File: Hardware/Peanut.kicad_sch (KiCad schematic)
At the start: 1 part

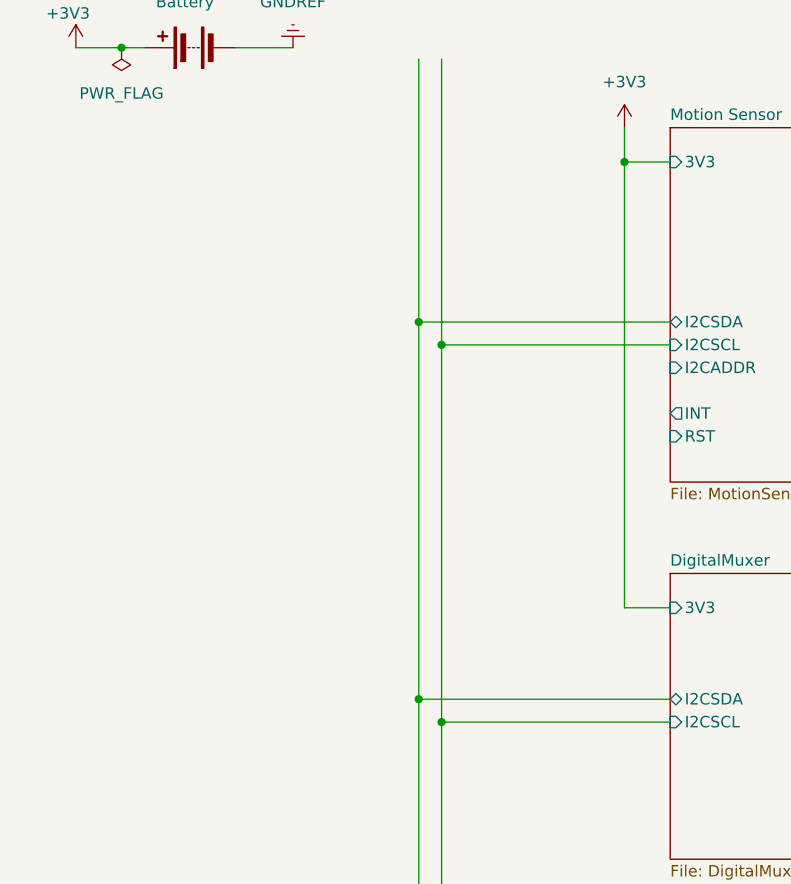
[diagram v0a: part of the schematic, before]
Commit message: Add Temperature and Humidity Sensor
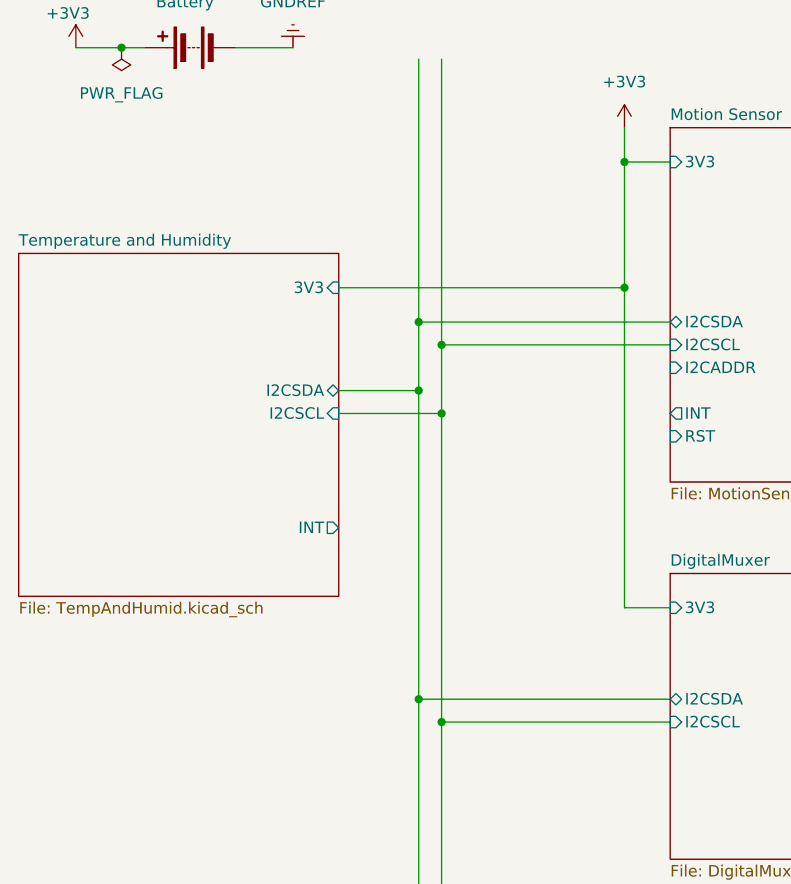
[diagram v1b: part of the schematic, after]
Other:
- added sheet Temperature and Humidity (TempAndHumid.kicad_sch)
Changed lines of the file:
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@@
+	)
+	(junction
+		(at 109.22 85.09)
+		(diameter 0)
+		(color 0 0 0 0)
+	)
+	(junction
+		(at 106.68 82.55)
+		(diameter 0)
+		(color 0 0 0 0)
+	)
+	(junction
+		(at 129.54 71.12)
+		(diameter 0)
+		(color 0 0 0 0)
 	)
 	(junction
@@
 	(wire
 		(pts
-			(xy 129.54 106.68) (xy 129.54 57.15)
+			(xy 97.79 71.12) (xy 129.54 71.12)
+		)
+		(stroke
+			(width 0)
+			(type default)
+		)
+	)
+	(wire
+		(pts
+			(xy 129.54 57.15) (xy 129.54 71.12)
 		)
 		(stroke
@@
 	(wire
 		(pts
+			(xy 97.79 82.55) (xy 106.68 82.55)
+		)
+		(stroke
+			(width 0)
+			(type default)
+		)
+	)
+	(wire
+		(pts
 			(xy 106.68 45.72) (xy 106.68 74.93)
 		)
@@
 	(wire
 		(pts
-			(xy 106.68 74.93) (xy 106.68 116.84)
+			(xy 106.68 74.93) (xy 106.68 82.55)
 		)
 		(stroke
@@
 	(wire
 		(pts
+			(xy 106.68 82.55) (xy 106.68 116.84)
+		)
+		(stroke
+			(width 0)
+			(type default)
+		)
+	)
+	(wire
+		(pts
+			(xy 129.54 71.12) (xy 129.54 106.68)
+		)
+		(stroke
+			(width 0)
+			(type default)
+		)
+	)
+	(wire
+		(pts
+			(xy 109.22 85.09) (xy 109.22 77.47)
+		)
+		(stroke
+			(width 0)
+			(type default)
+		)
+	)
+	(wire
+		(pts
 			(xy 134.62 106.68) (xy 129.54 106.68)
 		)
@@
 	(wire
 		(pts
+			(xy 97.79 85.09) (xy 109.22 85.09)
+		)
+		(stroke
+			(width 0)
+			(type default)
+		)
+	)
+	(wire
+		(pts
 			(xy 134.62 119.38) (xy 109.22 119.38)
 		)
@@
 	(wire
 		(pts
-			(xy 109.22 119.38) (xy 109.22 77.47)
+			(xy 109.22 85.09) (xy 109.22 119.38)
 		)
 		(stroke
@@
 				)
 			)
+		)
+	)
+	(sheet
+		(at 62.23 67.31)
+		(size 35.56 38.1)
+		(fields_autoplaced yes)
+		(stroke
+			(width 0.1524)
+			(type solid)
+		)
+		(fill
+			(color 255 229 191 1.0000)
+		)
+		(property "Sheetname" "Temperature and Humidity"
+			(at 62.23 66.5984 0)
+			(effects
+				(font
+					(size 1.27 1.27)
+				)
+				(justify left bottom)
+			)
+		)
+		(property "Sheetfile" "TempAndHumid.kicad_sch"
+			(at 62.23 105.9946 0)
+			(effects
+				(font
+					(size 1.27 1.27)
+				)
+				(justify left top)
+			)
+		)
+		(pin "3V3" input
+			(at 97.79 71.12 0)
+			(effects
+				(font
+					(size 1.27 1.27)
+				)
+				(justify right)
+			)
+		)
+		(pin "INT" output
+			(at 97.79 97.79 0)
+			(effects
+				(font
+					(size 1.27 1.27)
+				)
+				(justify right)
+			)
+		)
+		(pin "I2CSCL" input
+			(at 97.79 85.09 0)
+			(effects
+				(font
+					(size 1.27 1.27)
+				)
+				(justify right)
+			)
+		)
+		(pin "I2CSDA" bidirectional
+			(at 97.79 82.55 0)
+			(effects
+				(font
+					(size 1.27 1.27)
+				)
+				(justify right)
+			)
+		)
+		(instances
+			(project "Peanut"
+				(path "/298ef215-2a76-4225-b9ba-26c57869f278"
+					(page "4")
+				)
+			)

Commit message: Ambient Light Sensor
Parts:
- added J1: Conn_02x04_Odd_Even, symbol Connector_Generic:Conn_02x04_Odd_Even
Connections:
- net +3V3: now also J1.8 (Pin_8)
- net DigitalMuxer/I2CSCL: now also J1.4 (Pin_4)
- net DigitalMuxer/I2CSDA: now also J1.3 (Pin_3)
- new net GND: J1.1 (Pin_1)
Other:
- added sheet Light Sensor (LightSensor.kicad_sch)
- note added: "BOOT"
- note added: "RST"
- note added: "This is wrong"
- note added: "UART RX"
- note added: "UART TX"

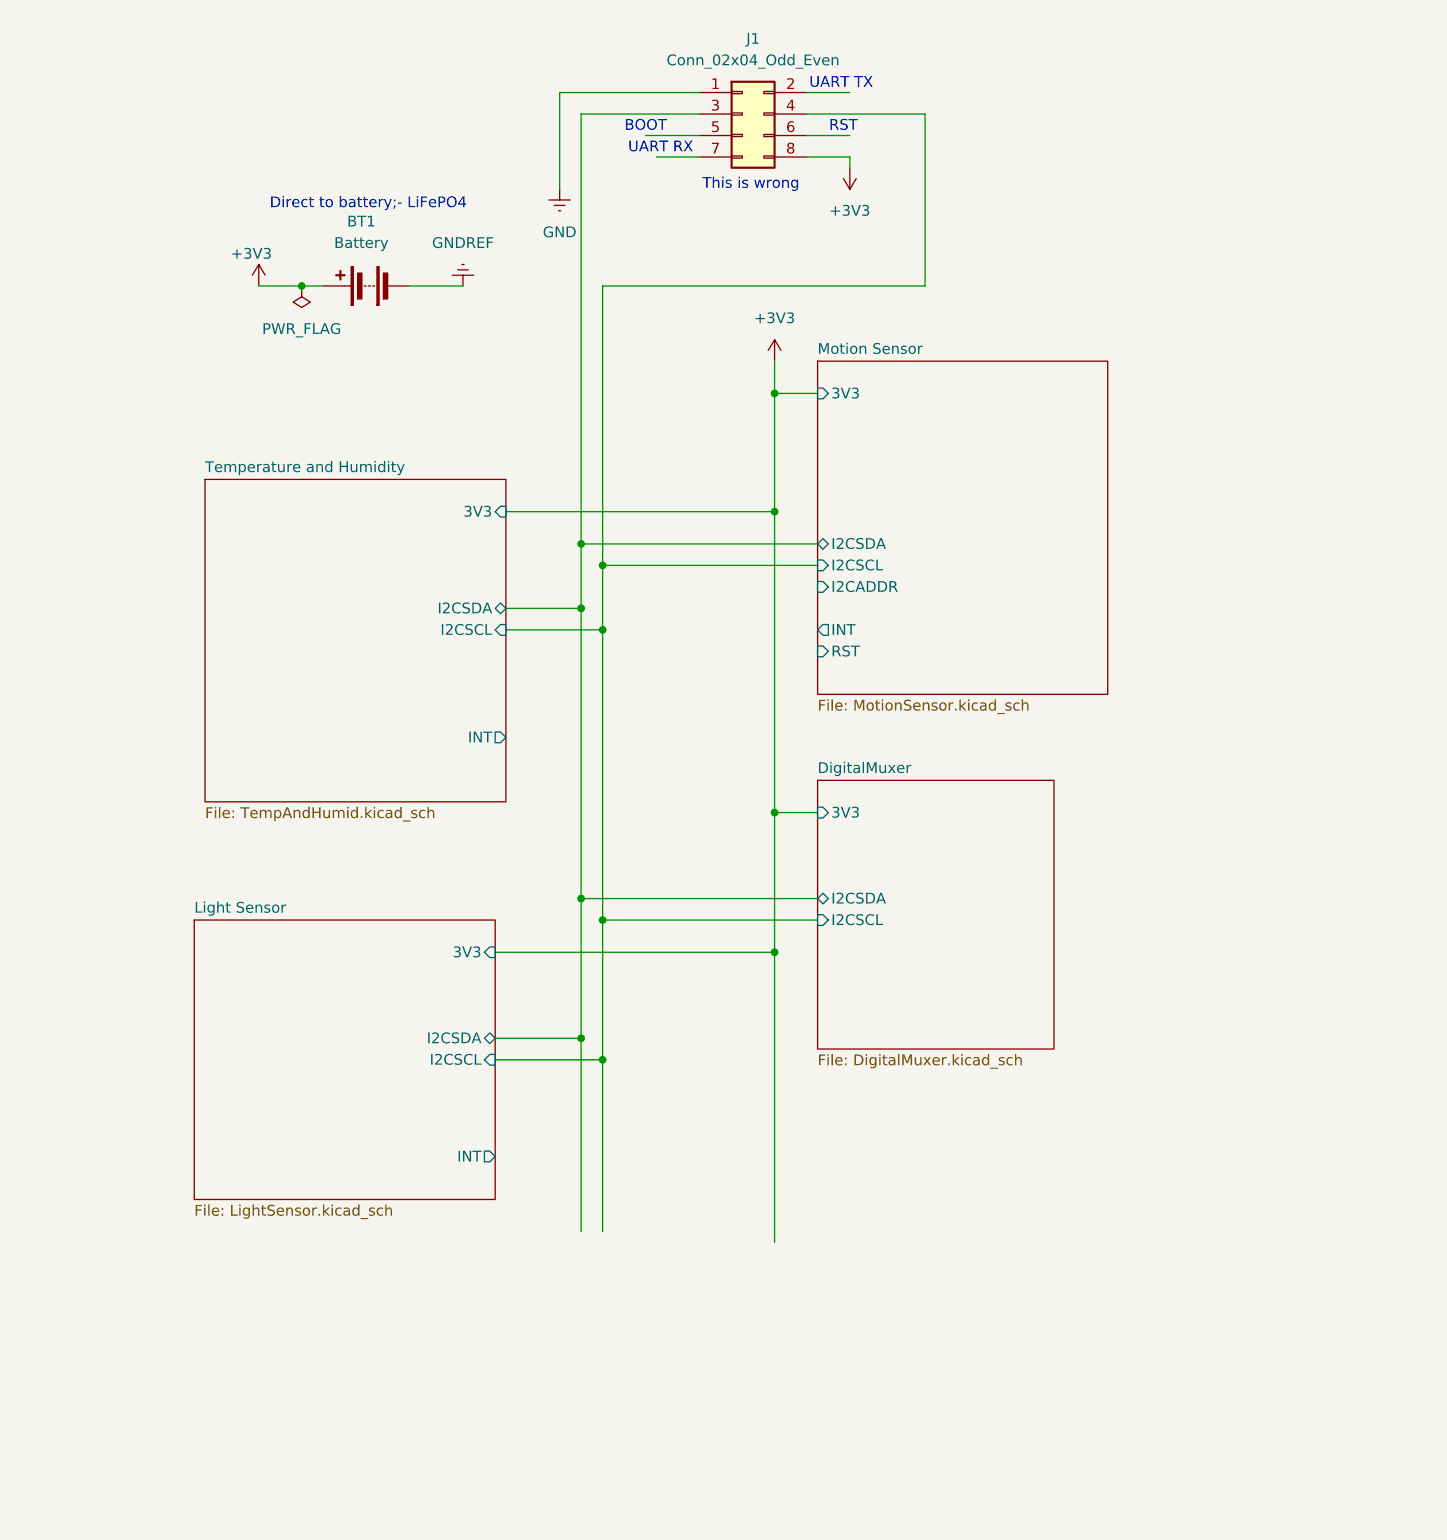
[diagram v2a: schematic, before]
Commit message: Use tags for nets, apply netgroups, mess around in pcb view
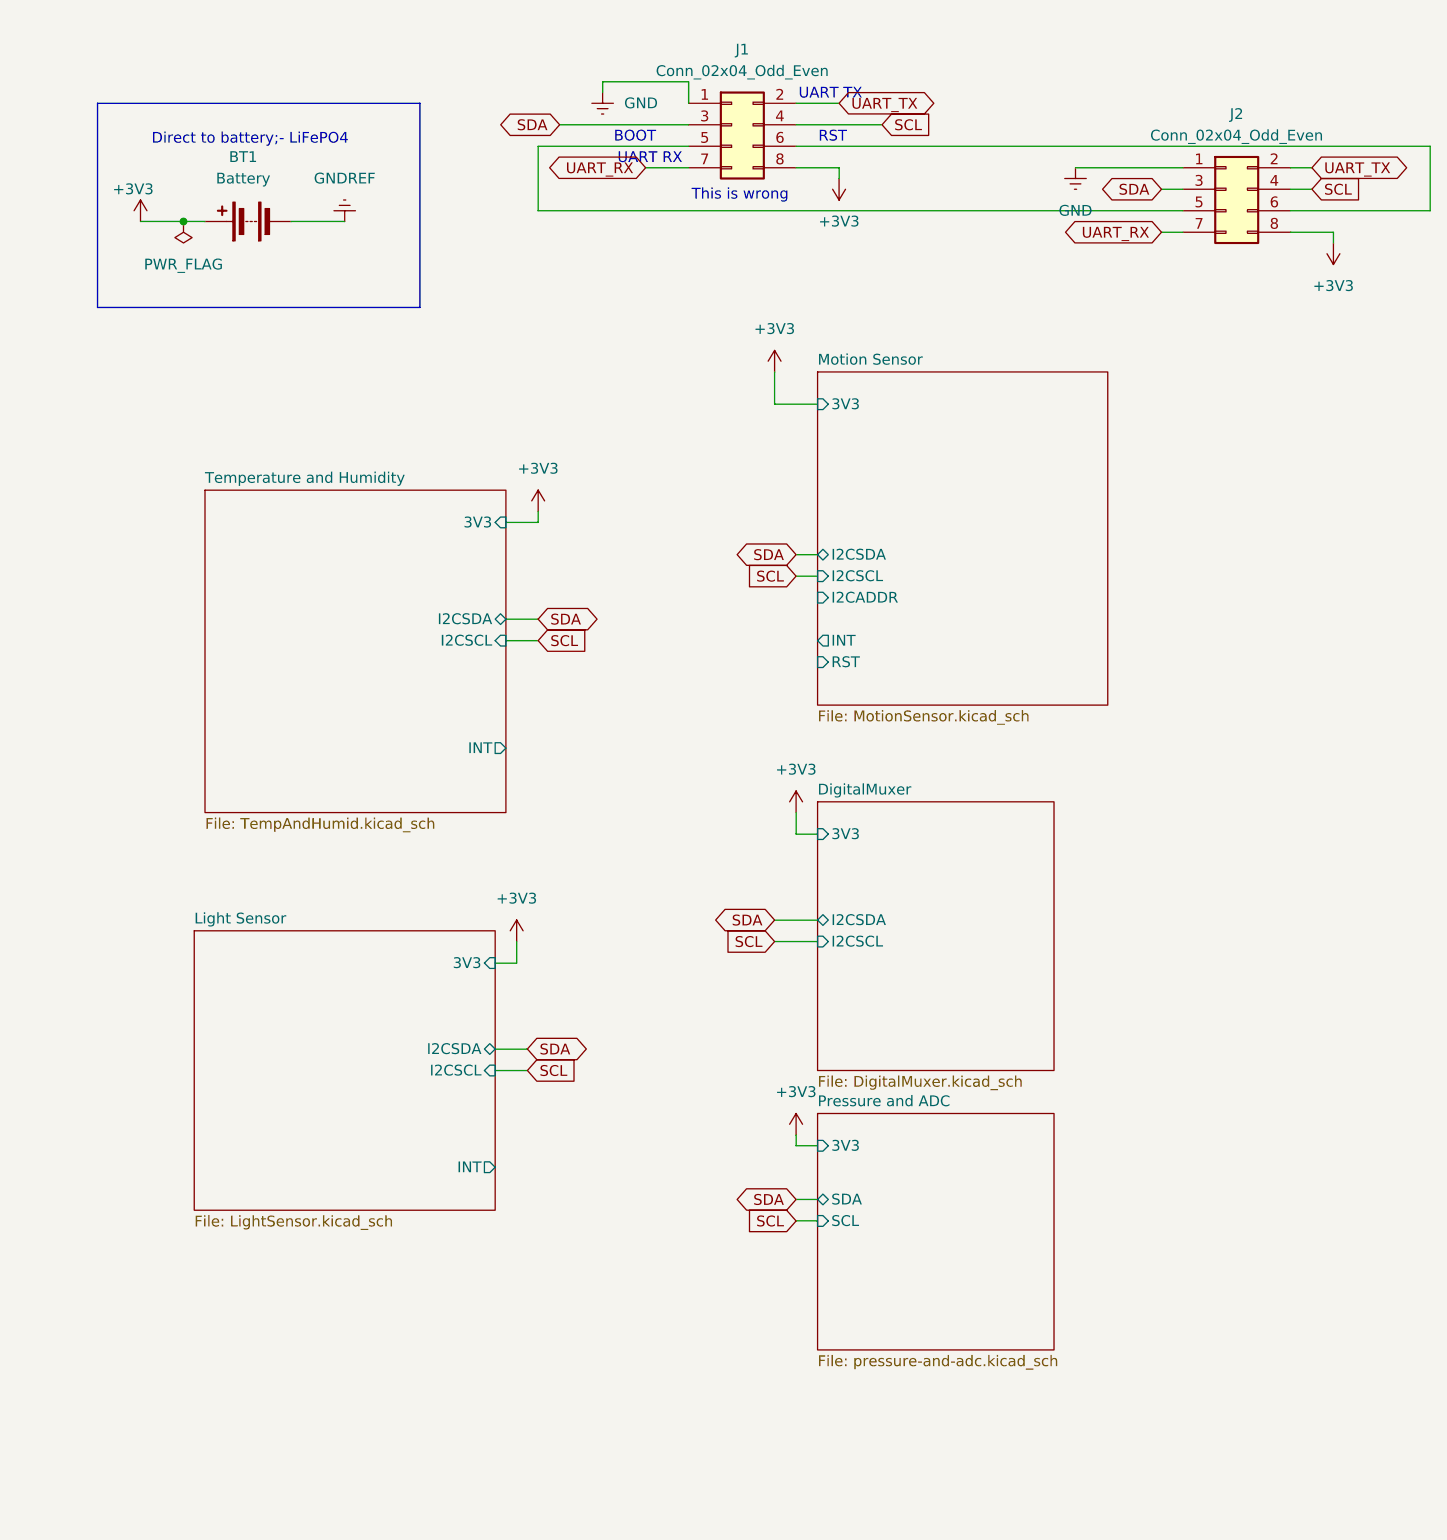
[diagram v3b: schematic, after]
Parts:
- added J2: Conn_02x04_Odd_Even, Connector_PinHeader_2.54mm:PinHeader_2x04_P2.54mm_Horizontal, symbol Connector_Generic:Conn_02x04_Odd_Even
- BT1: footprint (none) -> Battery:BatteryHolder_Keystone_2460_1xAA
- J1: footprint (none) -> Connector_PinSocket_2.54mm:PinSocket_2x04_P2.54mm_Vertical
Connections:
- net +3V3: now also J2.8 (Pin_8)
- net GND: now also J2.1 (Pin_1)
- net UART_TX: now reaches J1.2 (Pin_2)
- net UART_TX: now also J2.2 (Pin_2)
- net at J1.5 (Pin_5): now also J2.5 (Pin_5)
- net at J1.6 (Pin_6): now also J2.6 (Pin_6)
- net UART_RX: now reaches J1.7 (Pin_7)
- net UART_RX: now also J2.7 (Pin_7)
- net DigitalMuxer/I2CSCL renamed SCL
- net SCL: now also J2.4 (Pin_4)
- net DigitalMuxer/I2CSDA renamed SDA
- net SDA: now also J2.3 (Pin_3)
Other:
- added sheet Pressure and ADC (pressure-and-adc.kicad_sch)
- moved on the sheet: BT1, J1

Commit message: Use Peanut symbols, fix ERC errors, progress on DAC & Pressure
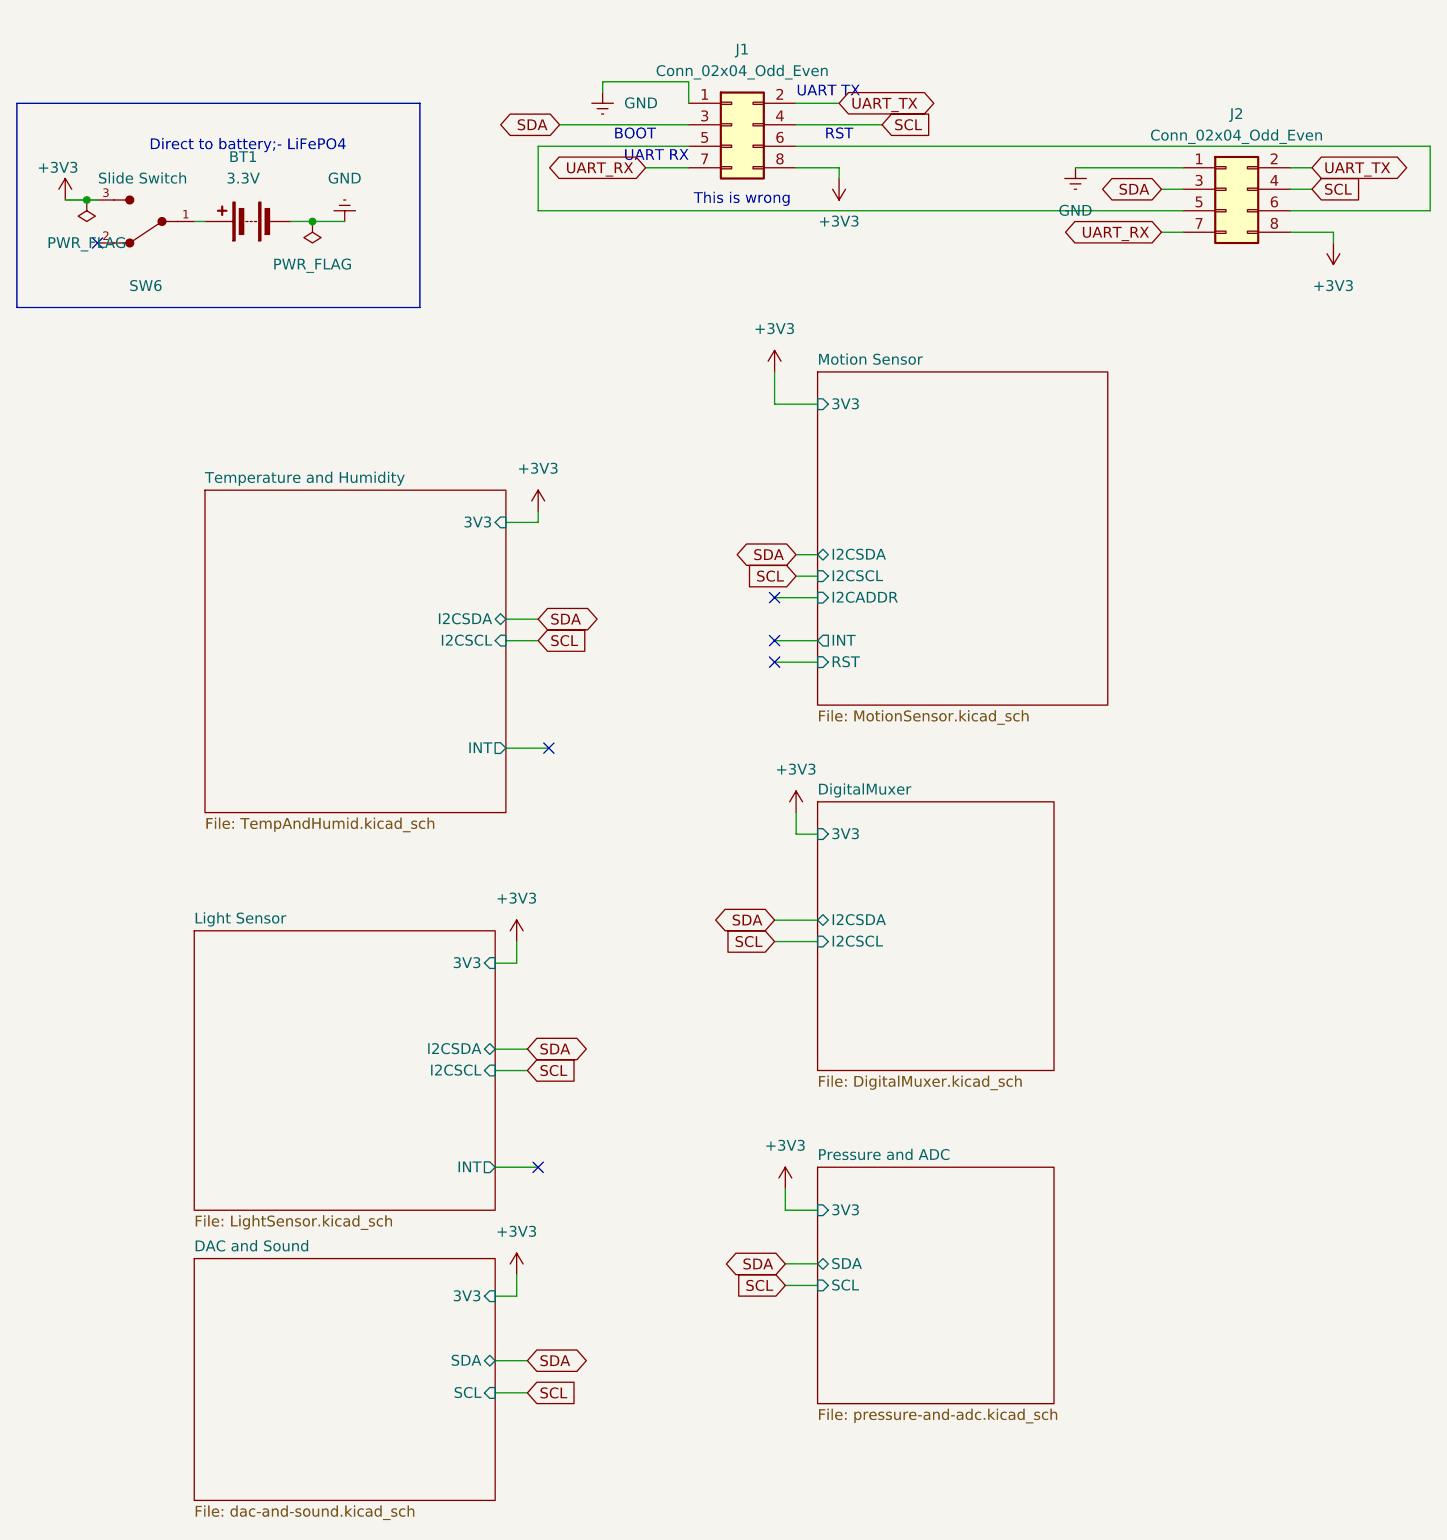
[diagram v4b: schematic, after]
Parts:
- added SW6: Slide Switch, Button_Switch_THT:SW_E-Switch_EG1224_SPDT_Angled, symbol Peanut:Slide_Switch_SPDT_P3mm_10x5x10mm
- BT1: value Battery -> 3.3V; footprint Battery:BatteryHolder_Keystone_2460_1xAA -> Battery:BatteryHolder_Keystone_1042_1x18650
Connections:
- net GNDREF is gone; now on net GND: BT1.2 (-)
- net +3V3: now also SW6.3; no longer BT1.1 (+)
- new net: BT1.1 (+), SW6.1
- no-connect marks 0 -> 6
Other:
- added sheet DAC and Sound (dac-and-sound.kicad_sch)
